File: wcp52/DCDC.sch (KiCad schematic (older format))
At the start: 55 parts, among them Q15 MMBT3904, Q16 MMBT3904, Q17 PZT2907A, Q18 PZT2907A, Q19 MMBT3904, Q20 MMBT3904, U13 L78M05CDT, U14 MC79M05CDT, U15 AZ1117CH-1.8TRG1, U16 MCP1700T-3302E/TT

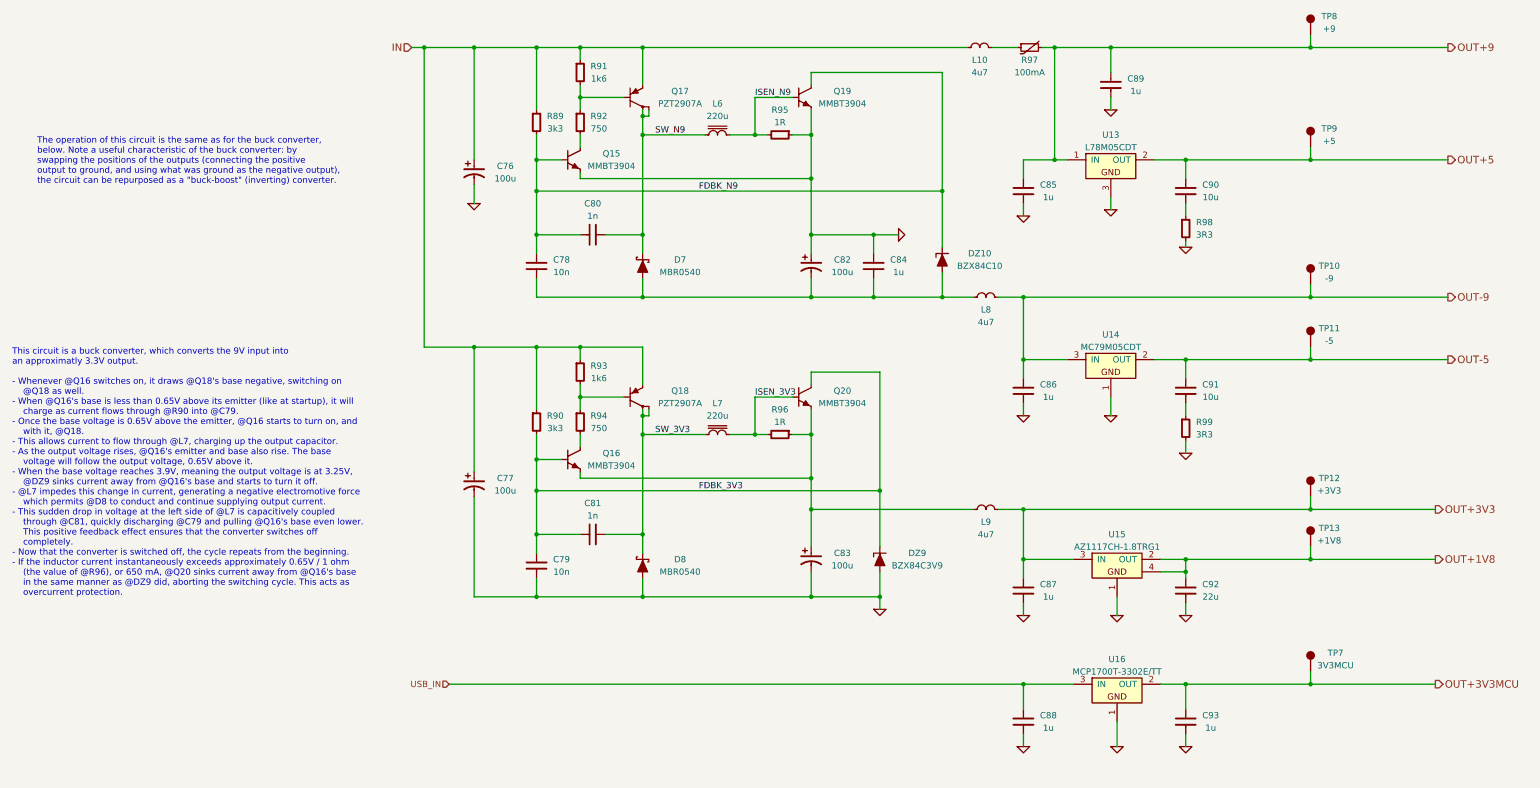
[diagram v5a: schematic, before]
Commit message: Change schematic pages to letter size
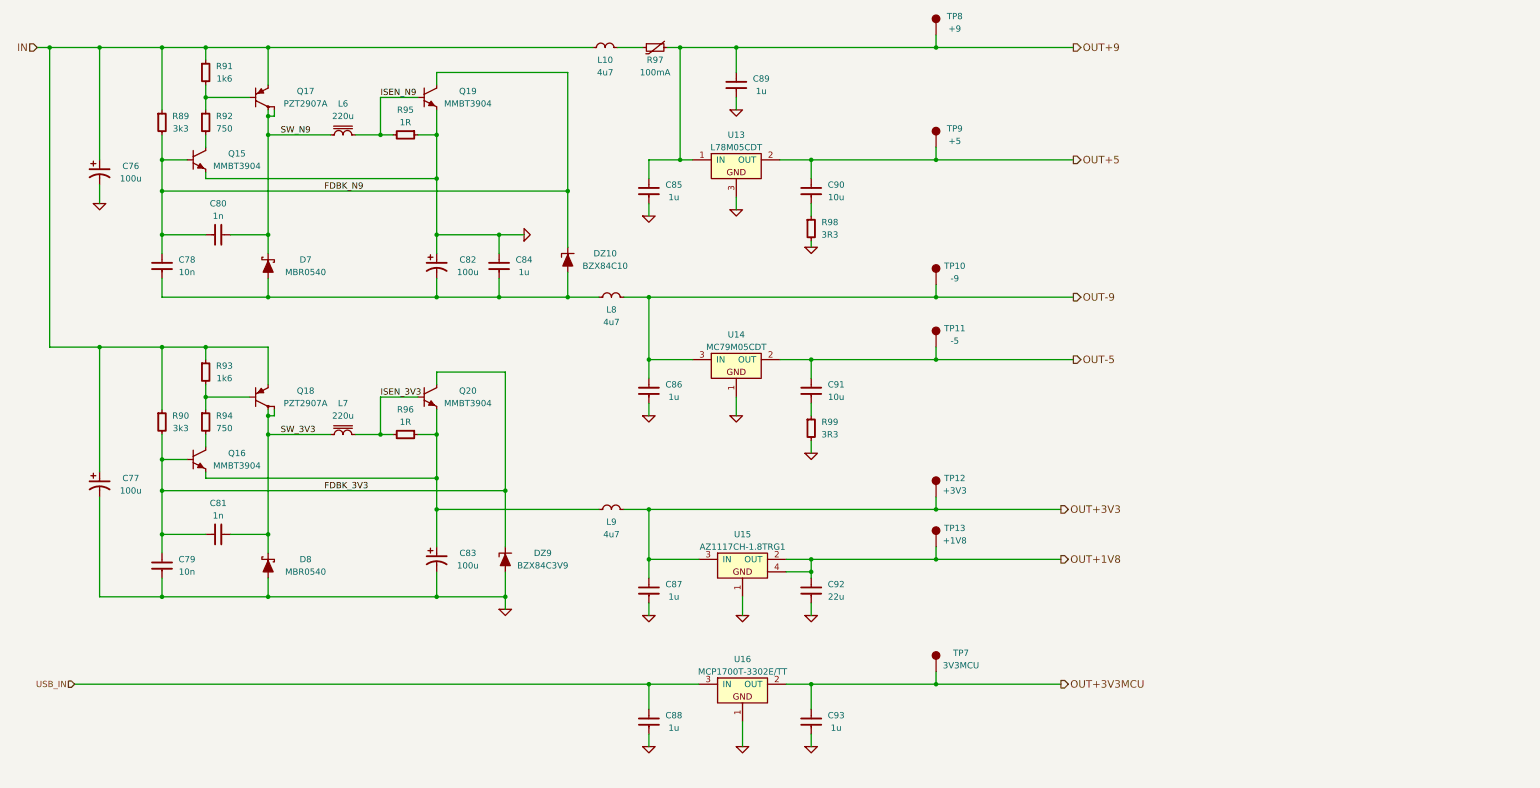
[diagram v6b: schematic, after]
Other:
- note removed: "The operation of this circuit is the same as for the buck converter,\nbelow. Note a useful characteristic of the buck converter: by\nswapping the positions of the outputs (connecting the positive\noutput to ground, and using what was ground as the negative output),\nthe circuit can be repurposed as a "buck-boost" (inverting) converter."
- note removed: "This circuit is a buck converter, which converts the 9V input into\nan approximatly 3.3V output.\n\n- Whenever @Q16 switches on, it draws @Q18's base negative, switching on\n @Q18 as well.\n- When @Q16's base is less than 0.65V above its emitter (like at startup), it will\n charge as current flows through @R90 into @C79.\n- Once the base voltage is 0.65V above the emitter, @Q16 starts to turn on,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"
- moved on the sheet: C76, C77, C78, C79, C80, C81, C82, C83, C84, C85, C86, C87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

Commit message: Correct BOM lines
The BOM reader currently cannot interpret things like '3k3'.
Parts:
- R91, R93: BOM RES SMD 1k6 1% [0603] -> RES SMD 1.6k 1% [0603]
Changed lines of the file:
@@
 F 3 "" H 2350 3650 60  0000 C CNN
 F 4 "Value" H 2350 3600 60  0001 C CNN "Manuf"
-F 5 "RES SMD 1k6 1% [0603]" H 3100 4150 60  0001 C CNN "BOM"
+F 5 "RES SMD 1.6k 1% [0603]" H 3100 4150 60  0001 C CNN "BOM"
 F 6 "R61" H 2350 3600 50  0001 C CNN "OldReference"
 	1    2350 3600
@@
 F 3 "" H 2350 1250 60  0000 C CNN
 F 4 "Value" H 2350 1200 60  0001 C CNN "Manuf"
-F 5 "RES SMD 1k6 1% [0603]" H 3100 1750 60  0001 C CNN "BOM"
+F 5 "RES SMD 1.6k 1% [0603]" H 3100 1750 60  0001 C CNN "BOM"
 F 6 "R65" H 2350 1200 50  0001 C CNN "OldReference"
 	1    2350 1200

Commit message: BOM fixes
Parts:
- U13: BOM DIST DIGIKEY 497-1203-1-ND -> IC ST L78M05CDT
- U14: BOM DIST DIGIKEY MC79M05CDTGOS-ND -> IC ONSEMI MC79M05CDTG
- U15: BOM DIST DIGIKEY AZ1117CH-1.8TRG1DICT-ND -> IC DIODES AZ1117CH-1.8TRG1
- U16: BOM DIST DIGIKEY MCP1700T3302ETTCT-ND -> IC MICROCHIP MCP1700T-3302E/TT; Manuf (none) -> Microchip; PN (none) -> MCP1700T-3302E/TT
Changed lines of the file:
@@
 EESchema Schematic File Version 2
-LIBS:Altera
-LIBS:AnalogDevices
-LIBS:Atmel
-LIBS:conn-2mm
-LIBS:conn-100mil
-LIBS:conn-cui
-LIBS:conn-fci
-LIBS:conn-linx
-LIBS:conn-molex
-LIBS:conn-tagconnect
-LIBS:conn-test
-LIBS:DiodesInc
-LIBS:display
-LIBS:_electromech
-LIBS:Fairchild
-LIBS:FTDI
-LIBS:Intersil
-LIBS:Lattice
-LIBS:_linear
-LIBS:LinearTech
-LIBS:Littelfuse
-LIBS:logic-4000
-LIBS:logic-7400
-LIBS:MACOM
-LIBS:maxim
-LIBS:mechanical
-LIBS:Microchip
-LIBS:Micron
-LIBS:NXP
-LIBS:onsemi
-LIBS:passive
-LIBS:pasv-BiTech
-LIBS:pasv-Bourns
-LIBS:pasv-cap
-LIBS:pasv-ind
-LIBS:pasv-res
-LIBS:pcb
-LIBS:power
-LIBS:_semi
-LIBS:semi-diode-1N
-LIBS:semi-diode-BA
-LIBS:semi-diode-MCC
-LIBS:semi-diode-MMB
-LIBS:semi-diode-NXP
-LIBS:semi-diode-OnSemi
-LIBS:semi-diode-Vishay
-LIBS:semi-opto-misc
-LIBS:semi-thyristor-2N
-LIBS:semi-trans-2N
-LIBS:semi-trans-AO
-LIBS:semi-trans-BC
-LIBS:semi-trans-DiodesInc
-LIBS:semi-trans-Fairchild
-LIBS:semi-trans-Infineon
-LIBS:semi-trans-IntRect
-LIBS:semi-trans-IXYS
-LIBS:semi-trans-misc
-LIBS:semi-trans-MMB
-LIBS:semi-trans-MPS
-LIBS:semi-trans-NXP
-LIBS:semi-trans-PZT
-LIBS:semi-trans-TI
-LIBS:semi-trans-TIP
-LIBS:semi-trans-Toshiba
-LIBS:silabs
-LIBS:skyworks
-LIBS:ST
-LIBS:st_ic
-LIBS:st_semi
-LIBS:supertex
-LIBS:symbol
-LIBS:TexasInstruments
-LIBS:vishay_semi
-LIBS:Xilinx
-LIBS:pasv-xtal
-LIBS:conn-te
 LIBS:wcp52-cache
 EELAYER 25 0
@@
 F 4 "L78M05CDT" H 6600 1450 50  0001 C CNN "PN"
 F 5 "ST" H 6600 1550 50  0001 C CNN "Manuf"
-F 6 "DIST DIGIKEY 497-1203-1-ND" H 6600 1350 50  0001 C CNN "BOM"
+F 6 "IC ST L78M05CDT" H 6600 1350 50  0001 C CNN "BOM"
 F 7 "U14" H 6600 1950 50  0001 C CNN "OldReference"
 	1    6600 1950
@@
 F 4 "MC79M05CDTG" H 6600 3050 50  0001 C CNN "PN"
 F 5 "ONSemi" H 6600 3150 50  0001 C CNN "Manuf"
-F 6 "DIST DIGIKEY MC79M05CDTGOS-ND" H 6600 2950 50  0001 C CNN "BOM"
+F 6 "IC ONSEMI MC79M05CDTG" H 6600 2950 50  0001 C CNN "BOM"
 F 7 "U15" H 6600 3550 50  0001 C CNN "OldReference"
 	1    6600 3550
@@
 F 4 "AZ1117CH-1.8TRG1" H 6650 5150 60  0001 C CNN "PN"
 F 5 "DiodesInc" H 6650 5150 60  0001 C CNN "Manuf"
-F 6 "DIST DIGIKEY AZ1117CH-1.8TRG1DICT-ND" H 6650 5150 60  0001 C CNN "BOM"
+F 6 "IC DIODES AZ1117CH-1.8TRG1" H 6650 5150 60  0001 C CNN "BOM"
 F 7 "U16" H 6650 5150 50  0001 C CNN "OldReference"
 	1    6650 5150
@@
 F 2 "smd-semi:SOT-23" H 6650 6150 60  0001 C CNN
 F 3 "" H 6650 6150 60  0000 C CNN
-F 4 "DIST DIGIKEY MCP1700T3302ETTCT-ND" H 6650 6150 60  0001 C CNN "BOM"
-F 5 "U17" H 6650 6150 50  0001 C CNN "OldReference"
+F 4 "MCP1700T-3302E/TT" H 6650 6150 60  0001 C CNN "PN"
+F 5 "Microchip" H 6650 6150 60  0001 C CNN "Manuf"
+F 6 "IC MICROCHIP MCP1700T-3302E/TT" H 6650 6150 60  0001 C CNN "BOM"
+F 7 "U17" H 6650 6150 50  0001 C CNN "OldReference"
 	1    6650 6150
 	1    0    0    -1
